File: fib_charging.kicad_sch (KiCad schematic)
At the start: 42 parts, among them J301 Conn_01x02, J302 Conn_01x02, J303 Conn_01x02, Q301 CSD17581Q3A, Q302 CSD17581Q3A, Q303 CSD17581Q3A, Q304 CSD17581Q3A, U301 BQ25798RQMR

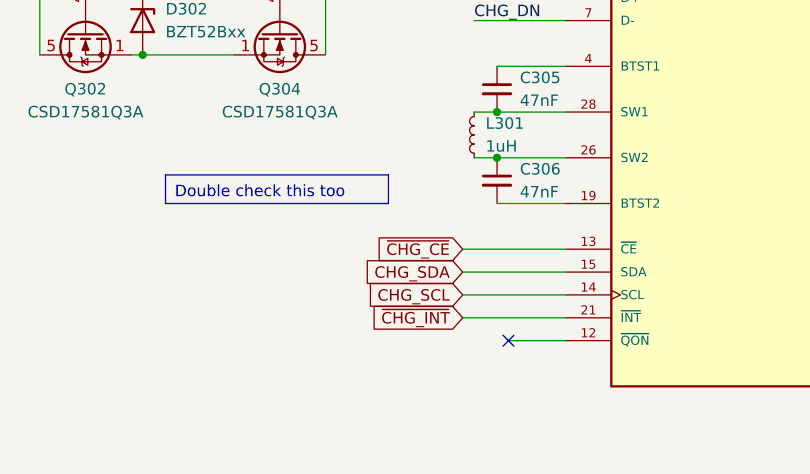
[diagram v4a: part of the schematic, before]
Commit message: continuing schematic work for pcie and other high speed interfaces
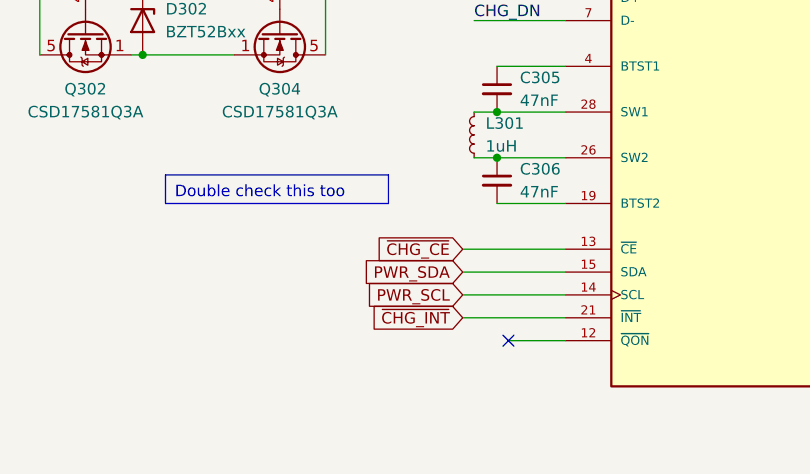
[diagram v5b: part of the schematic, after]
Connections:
- net CHG_SCL renamed PWR_SCL
- net CHG_SDA renamed PWR_SDA
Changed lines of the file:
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@@
 		)
 	)
-	(global_label "CHG_SCL"
+	(global_label "PWR_SCL"
 		(shape input)
 		(at 123.19 83.82 180)
@@
 		)
 		(property "Intersheetrefs" "${INTERSHEET_REFS}"
-			(at 111.8591 83.82 0)
+			(at 111.7382 83.82 0)
 			(effects
 				(font
@@
 		)
 	)
-	(global_label "CHG_SDA"
+	(global_label "PWR_SDA"
 		(shape input)
 		(at 123.19 81.28 180)
@@
 		)
 		(property "Intersheetrefs" "${INTERSHEET_REFS}"
-			(at 111.7986 81.28 0)
+			(at 111.6777 81.28 0)
 			(effects
 				(font

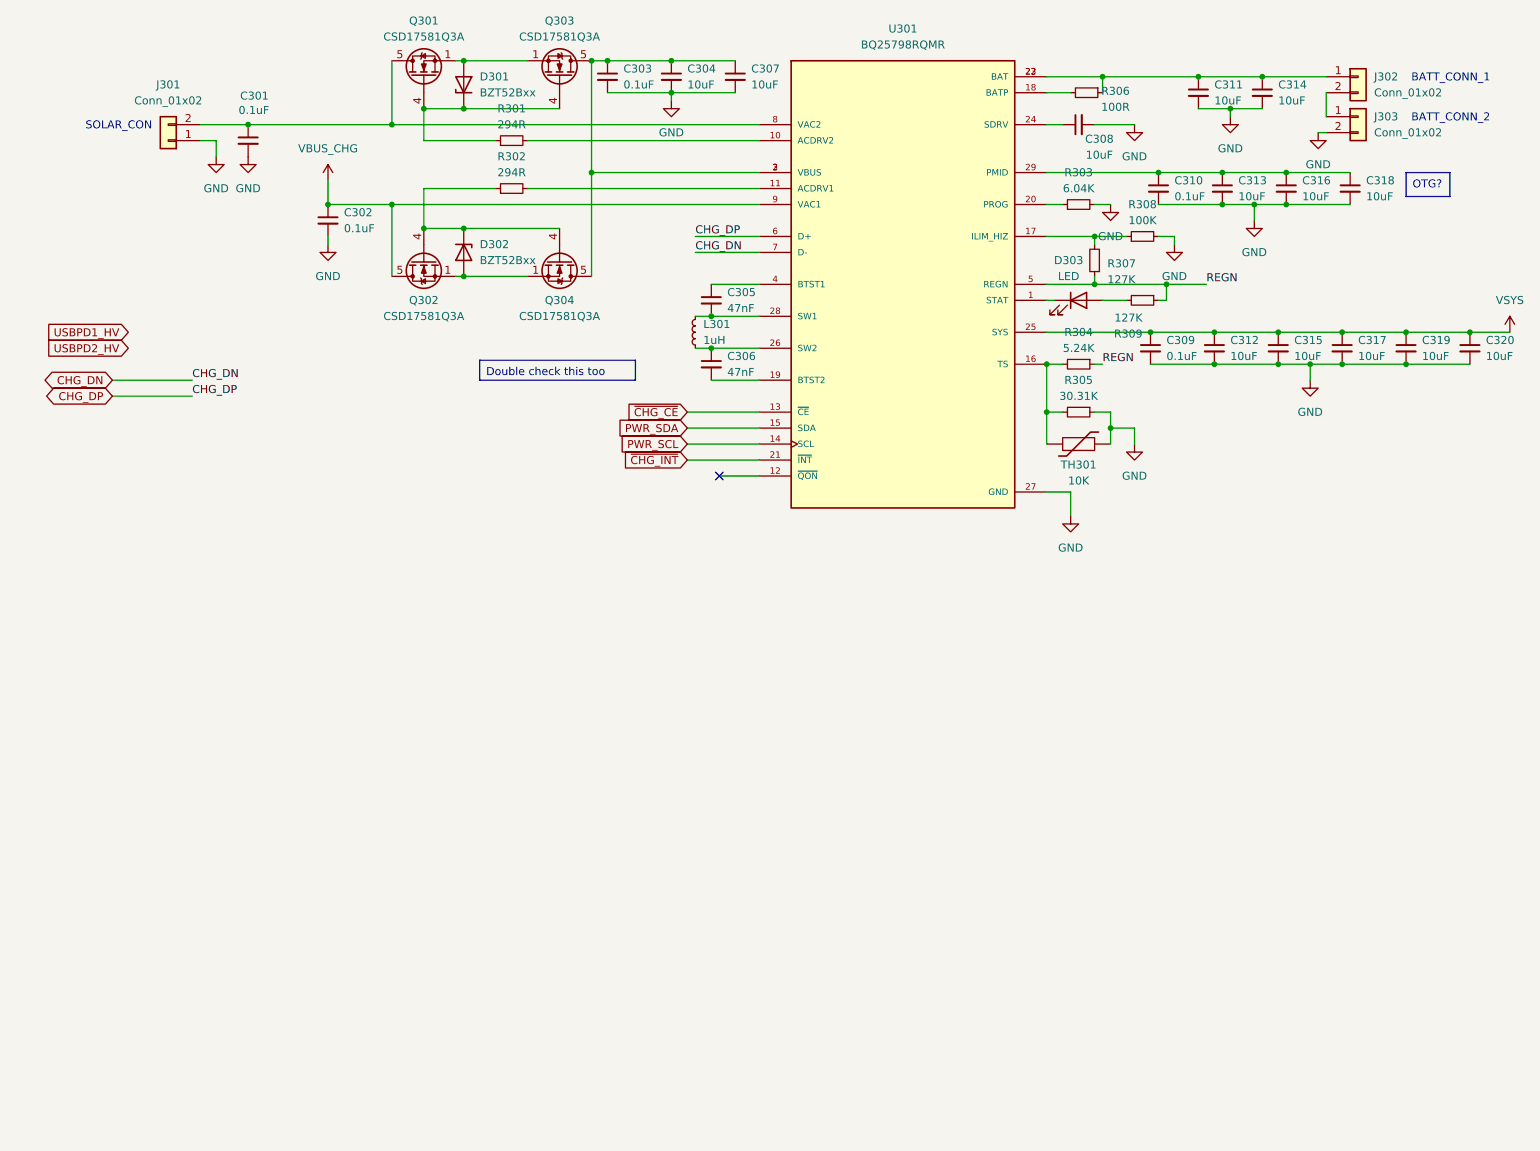
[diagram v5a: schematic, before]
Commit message: restructured EPD side of things, replaced rp2040 with esp32 s3 because of it's LCD controller, USB, LP WIFI_BT & EPDiy compat, repurposed USB0 for ESP interfacing, added e-ink pmic
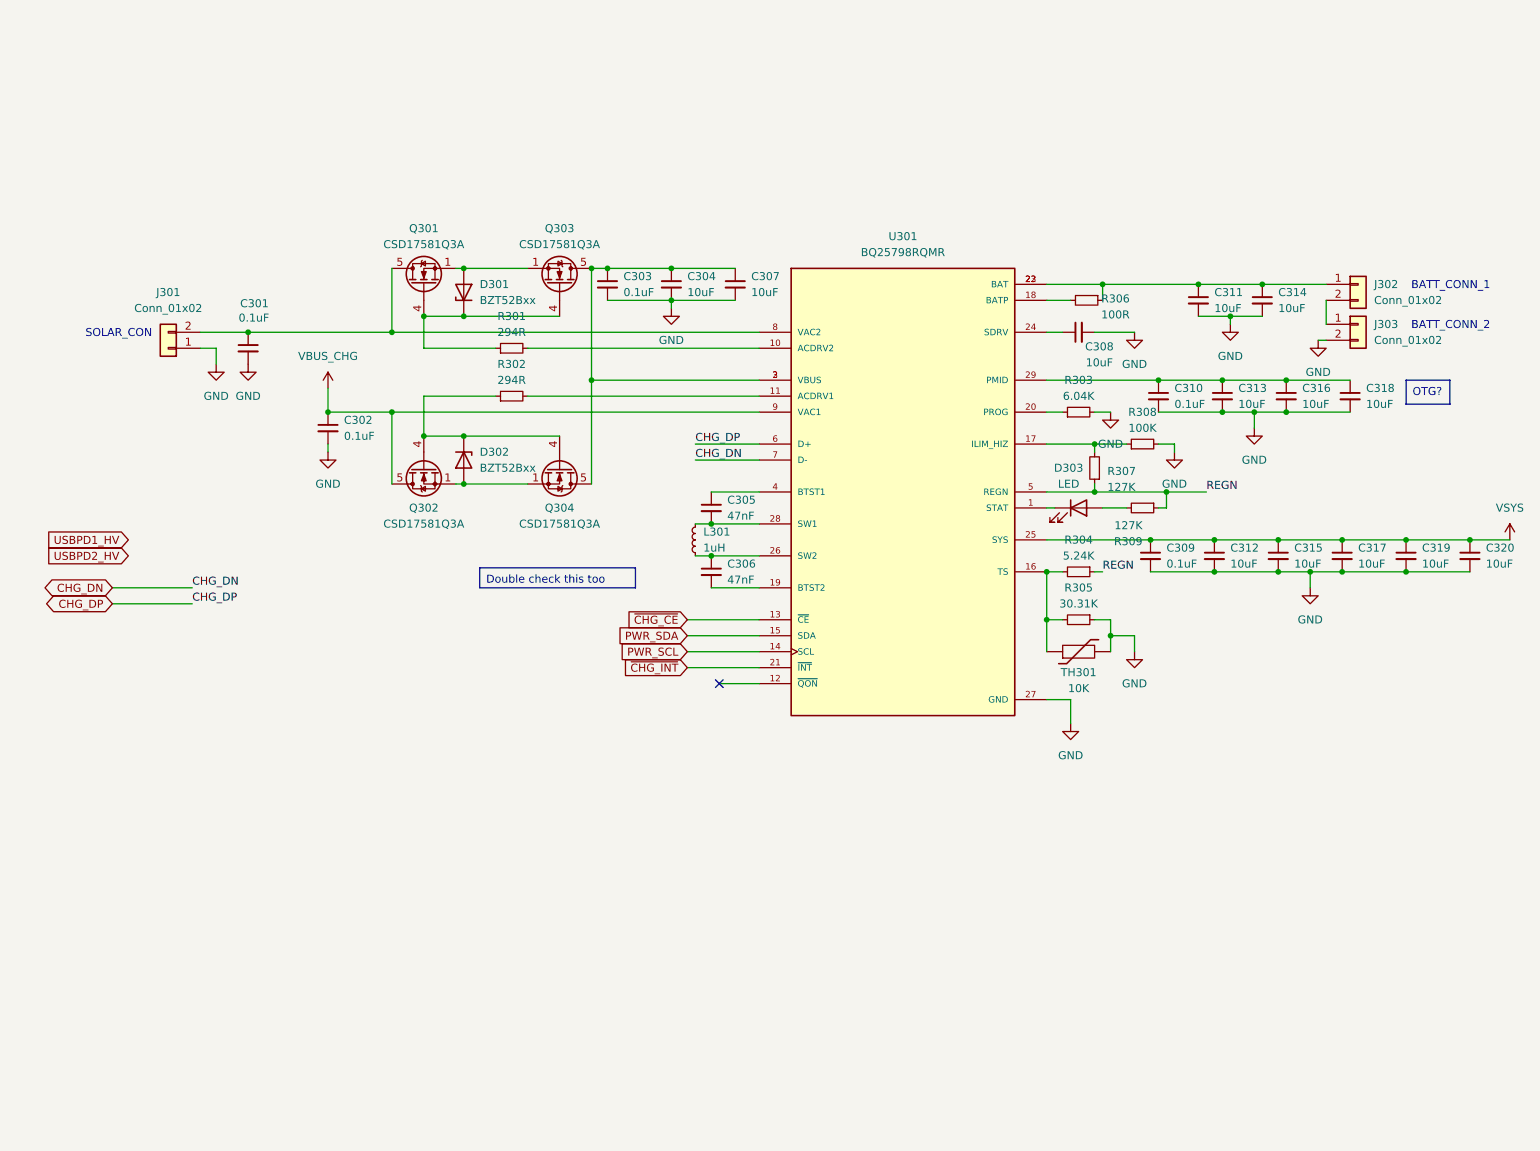
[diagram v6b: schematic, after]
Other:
- moved on the sheet: C301, C302, C303, C304, C305, C306, C307, C308, C309, C310, C311, C312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

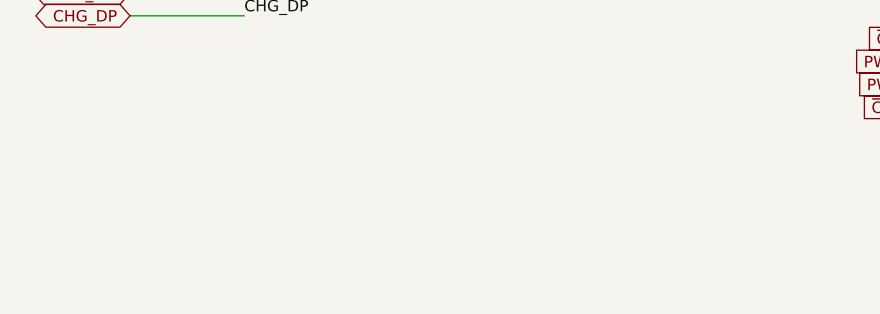
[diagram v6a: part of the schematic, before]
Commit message: added notest regarding the audio codec
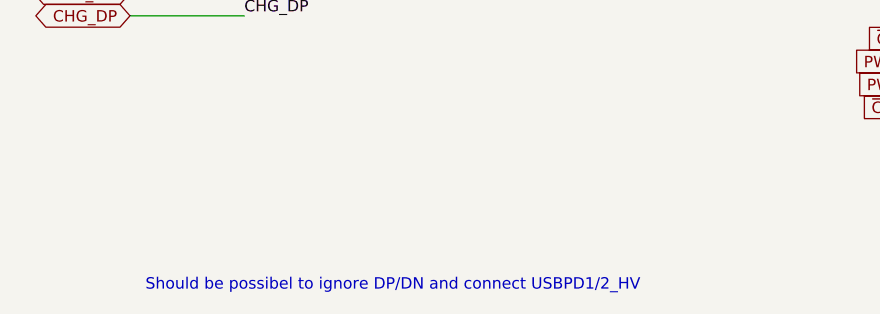
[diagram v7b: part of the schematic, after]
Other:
- note added: "Should be possibel to ignore DP/DN and connect USBPD1/2_HV"
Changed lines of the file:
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@@
+		)
+	)
+	(text "Should be possibel to ignore DP/DN and connect USBPD1/2_HV"
+		(exclude_from_sim no)
+		(at 60.96 139.192 0)
+		(effects
+			(font
+				(size 1.27 1.27)
+			)
 		)
 	)

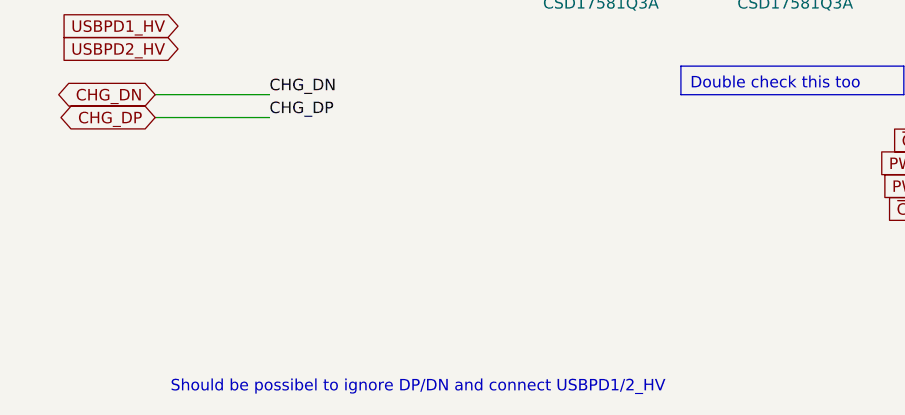
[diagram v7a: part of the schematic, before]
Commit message: added buck converter, refactoored peripherals and updated gpio/SPI/i2c mapping
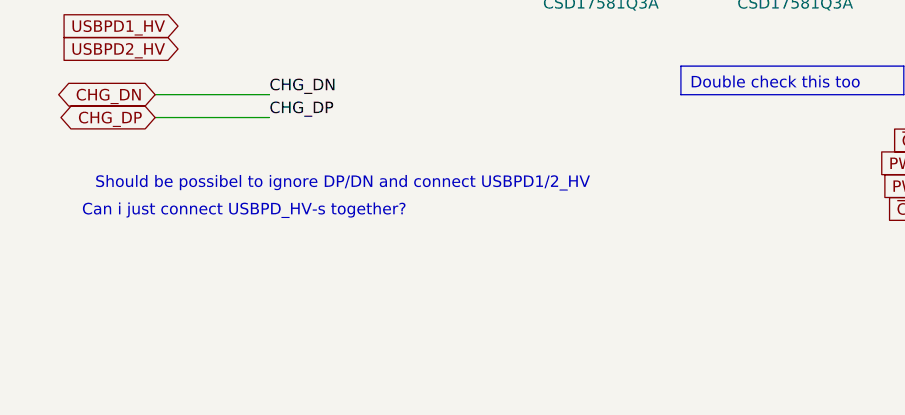
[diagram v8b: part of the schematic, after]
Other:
- note added: "Can i just connect USBPD_HV-s together?"
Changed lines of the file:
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@@
+		)
+	)
+	(text "Can i just connect USBPD_HV-s together?"
+		(exclude_from_sim no)
+		(at 41.656 119.634 0)
+		(effects
+			(font
+				(size 1.27 1.27)
+			)
 		)
 	)
 	(text "Should be possibel to ignore DP/DN and connect USBPD1/2_HV"
 		(exclude_from_sim no)
-		(at 60.96 139.192 0)
+		(at 52.578 116.586 0)
 		(effects
 			(font
